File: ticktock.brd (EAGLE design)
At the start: 61 x 67.3 mm, 64 parts, among them IC1 ATMEGA644A, IC2 AD8611RM, IC3 REF200U, J1 AVR_SPI_PRG_6NS, Q1 MOSFET-NCHANNEL2N7002PW, Q2 MOSFET-NCHANNELBSS138, Q3 MOSFET-NCHANNELBSS138, U1 MAX232SOIC16, U2 OSCILLATORSMD, U3 FT232RLSSOP, U4 BMP180, X1 RS232

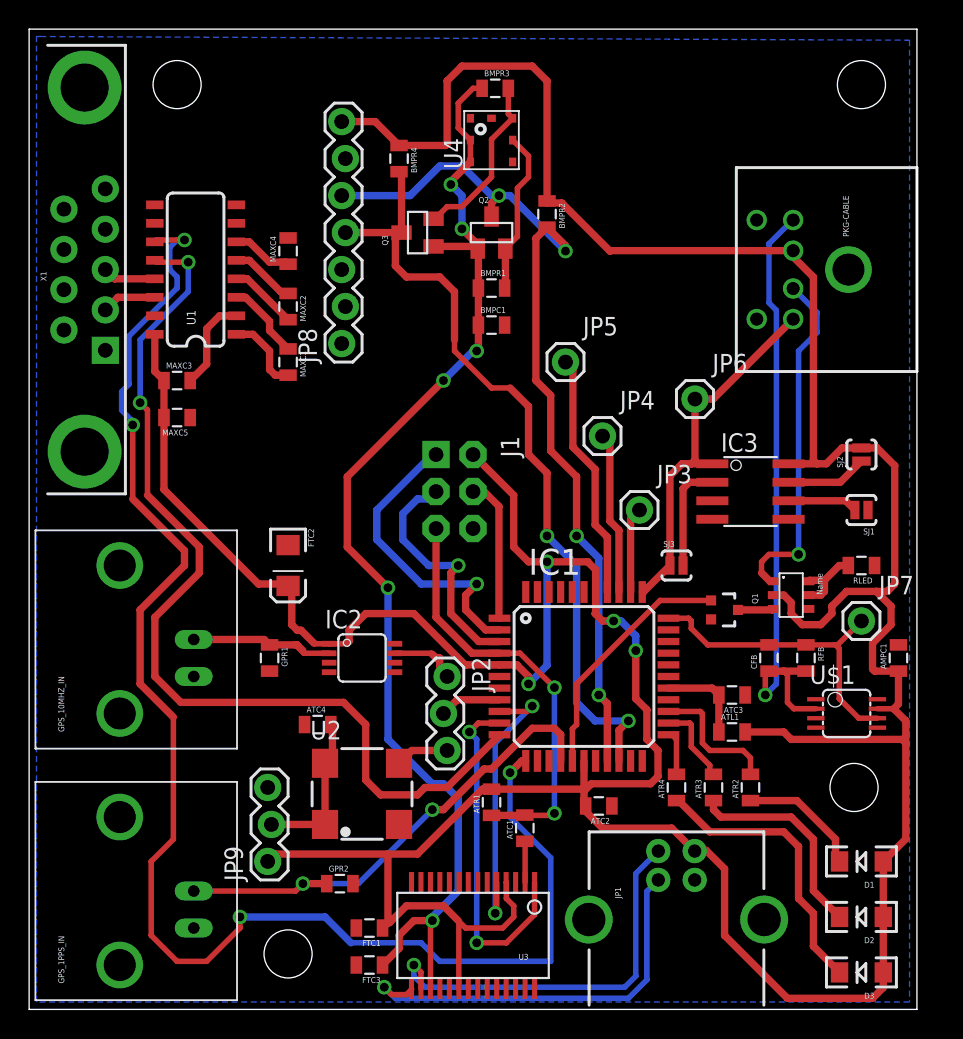
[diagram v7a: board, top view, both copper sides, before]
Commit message: Add top ground plane
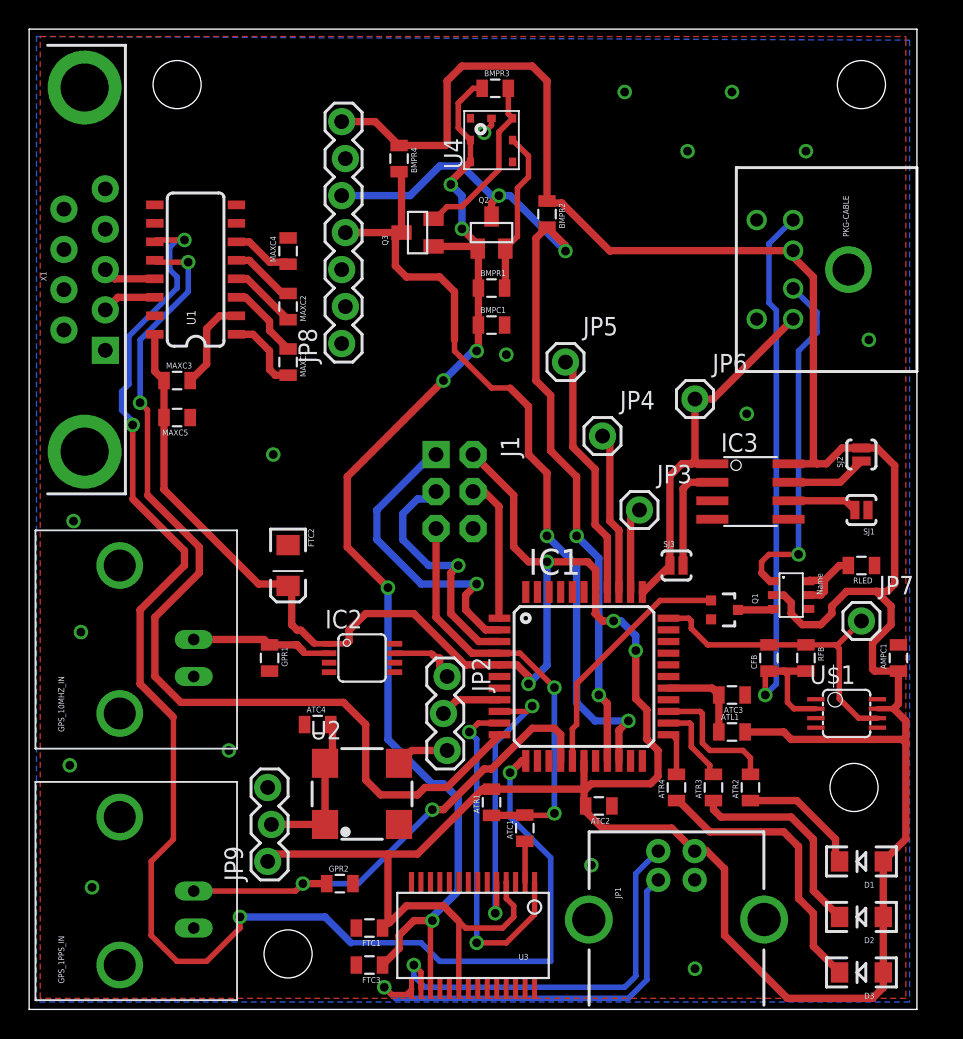
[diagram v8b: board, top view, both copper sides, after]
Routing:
- net GND: track 0.00 -> 1.20 mm, vias 0 -> 15
- added copper zone on layer 1, net GND
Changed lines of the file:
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@@
 <layers>
 <layer number="1" name="Top" color="4" fill="1" visible="yes" active="yes"/>
-<layer number="16" name="Bottom" color="1" fill="1" visible="yes" active="yes"/>
+<layer number="16" name="Bottom" color="1" fill="1" visible="no" active="yes"/>
 <layer number="17" name="Pads" color="2" fill="1" visible="yes" active="yes"/>
 <layer number="18" name="Vias" color="2" fill="1" visible="yes" active="yes"/>
@@
 <vertex x="0.508" y="66.802"/>
 </polygon>
-<wire x1="32.65" y1="46.99" x2="31.75" y2="61.19" width="0" layer="19" extent="1-1"/>
-<wire x1="21.463" y1="45.72" x2="32.65" y2="46.99" width="0" layer="19" extent="1-1"/>
-<wire x1="16.51" y1="23.23" x2="11.303" y2="22.86" width="0" layer="19" extent="1-1"/>
-<wire x1="20.597" y1="23.156" x2="16.51" y2="23.23" width="0" layer="19" extent="1-1"/>
-<wire x1="20.597" y1="23.806" x2="20.597" y2="23.156" width="0" layer="19" extent="1-1"/>
-<wire x1="18.912" y1="19.558" x2="20.597" y2="23.156" width="0" layer="19" extent="1-1"/>
-<wire x1="25.122" y1="23.806" x2="20.597" y2="23.806" width="0" layer="19" extent="1-1"/>
-<wire x1="25.122" y1="23.156" x2="25.122" y2="23.806" width="0" layer="19" extent="1-1"/>
-<wire x1="32.3" y1="22.86" x2="25.122" y2="23.156" width="0" layer="19" extent="1-1"/>
-<wire x1="40.016" y1="13.97" x2="45.7" y2="8.89" width="0" layer="19" extent="1-1"/>
-<wire x1="38.9" y1="17.06" x2="40.016" y2="13.97" width="0" layer="19" extent="1-1"/>
-<wire x1="43.9" y1="22.86" x2="38.9" y2="17.06" width="0" layer="19" extent="1-1"/>
-<wire x1="46.827" y1="26.782" x2="43.9" y2="22.86" width="0" layer="19" extent="1-1"/>
+<polygon width="0.254" layer="1" isolate="0.6096">
+<vertex x="0.762" y="66.802"/>
+<vertex x="60.198" y="66.802"/>
+<vertex x="60.198" y="66.548"/>
+<vertex x="60.198" y="0.762"/>
+<vertex x="0.762" y="0.762"/>
+</polygon>
+<via x="32.766" y="44.958" extent="1-16" drill="0.6"/>
+<wire x1="31.75" y1="61.19" x2="31.75" y2="60.706" width="0.381" layer="1"/>
+<wire x1="31.75" y1="60.706" x2="31.242" y2="60.198" width="0.381" layer="1"/>
+<via x="31.242" y="60.198" extent="1-16" drill="0.6"/>
+<via x="40.894" y="62.992" extent="1-16" drill="0.6"/>
+<via x="48.26" y="62.992" extent="1-16" drill="0.6"/>
+<via x="45.212" y="58.928" extent="1-16" drill="0.6"/>
+<via x="53.34" y="58.928" extent="1-16" drill="0.6"/>
+<via x="57.658" y="45.974" extent="1-16" drill="0.6"/>
+<via x="45.72" y="2.794" extent="1-16" drill="0.6"/>
+<via x="38.608" y="9.906" extent="1-16" drill="0.6"/>
+<via x="13.716" y="17.78" extent="1-16" drill="0.6"/>
+<via x="4.318" y="8.382" extent="1-16" drill="0.6"/>
+<via x="2.794" y="16.764" extent="1-16" drill="0.6"/>
+<via x="3.556" y="25.908" extent="1-16" drill="0.6"/>
+<via x="3.048" y="33.528" extent="1-16" drill="0.6"/>
+<via x="16.764" y="38.1" extent="1-16" drill="0.6"/>
+<wire x1="58.05" y1="30.48" x2="59.69" y2="25.03" width="0" layer="19" extent="1-1"/>
+<wire x1="53.524" y1="27.498" x2="58.05" y2="30.48" width="0" layer="19" extent="1-1"/>
+<wire x1="46.827" y1="26.782" x2="53.524" y2="27.498" width="0" layer="19" extent="1-1"/>
+<wire x1="43.9" y1="22.86" x2="46.827" y2="26.782" width="0" layer="19" extent="1-1"/>
 <wire x1="49.16" y1="21.59" x2="43.9" y2="22.86" width="0" layer="19" extent="1-1"/>
 <wire x1="54.021" y1="19.996" x2="49.16" y2="21.59" width="0" layer="19" extent="1-1"/>
 <wire x1="54.021" y1="19.346" x2="54.021" y2="19.996" width="0" layer="19" extent="1-1"/>
-<wire x1="53.524" y1="27.498" x2="46.827" y2="26.782" width="0" layer="19" extent="1-1"/>
-<wire x1="58.05" y1="30.48" x2="53.524" y2="27.498" width="0" layer="19" extent="1-1"/>
-<wire x1="57.6" y1="34.29" x2="58.05" y2="30.48" width="0" layer="19" extent="1-1"/>
-<wire x1="59.69" y1="25.03" x2="58.05" y2="30.48" width="0" layer="19" extent="1-1"/>
-<wire x1="17.78" y1="52.97" x2="21.463" y2="45.72" width="0" layer="19" extent="1-1"/>
-<wire x1="38.1" y1="28.66" x2="32.3" y2="22.86" width="0" layer="19" extent="1-1"/>
-<wire x1="17.78" y1="31.88" x2="20.597" y2="23.806" width="0" layer="19" extent="1-1"/>
-<wire x1="8.63" y1="47.625" x2="5.23" y2="56.34" width="0" layer="19" extent="1-1"/>
-<wire x1="11.06" y1="40.64" x2="8.63" y2="47.625" width="0" layer="19" extent="1-1"/>
-<wire x1="25.4" y1="12.7" x2="18.912" y2="19.558" width="0" layer="19" extent="1-1"/>
+<wire x1="38.9" y1="17.06" x2="43.9" y2="22.86" width="0" layer="19" extent="1-1"/>
+<wire x1="40.016" y1="13.97" x2="38.9" y2="17.06" width="0" layer="19" extent="1-1"/>
+<wire x1="38.608" y1="9.906" x2="40.016" y2="13.97" width="0" layer="19" extent="1-1"/>
+<wire x1="25.122" y1="23.806" x2="25.122" y2="23.156" width="0" layer="19" extent="1-1"/>
+<wire x1="20.597" y1="23.806" x2="20.597" y2="23.156" width="0" layer="19" extent="1-1"/>
+<wire x1="32.3" y1="22.86" x2="25.122" y2="23.156" width="0" layer="19" extent="1-1"/>
+<wire x1="30.805" y1="8.736" x2="38.608" y2="9.906" width="0" layer="19" extent="1-1"/>
+<wire x1="25.4" y1="12.7" x2="30.805" y2="8.736" width="0" layer="19" extent="1-1"/>
 <wire x1="22.236" y1="8.636" x2="25.4" y2="12.7" width="0" layer="19" extent="1-1"/>
-<wire x1="22.468" y1="5.588" x2="22.236" y2="8.636" width="0" layer="19" extent="1-1"/>
-<wire x1="22.468" y1="3.048" x2="22.468" y2="5.588" width="0" layer="19" extent="1-1"/>
 <wire x1="28.205" y1="1.424" x2="22.468" y2="3.048" width="0" layer="19" extent="1-1"/>
 <wire x1="30.155" y1="1.424" x2="28.205" y2="1.424" width="0" layer="19" extent="1-1"/>
 <wire x1="32.755" y1="1.424" x2="30.155" y2="1.424" width="0" layer="19" extent="1-1"/>
 <wire x1="33.405" y1="1.424" x2="32.755" y2="1.424" width="0" layer="19" extent="1-1"/>
-<wire x1="30.805" y1="8.736" x2="25.4" y2="12.7" width="0" layer="19" extent="1-1"/>
+<wire x1="38.1" y1="28.66" x2="43.9" y2="22.86" width="0" layer="19" extent="1-1"/>
 </signal>
 <signal name="IR_PWM">
@@
 <contactref element="Q3" pad="2"/>
 <contactref element="U4" pad="6"/>
-<wire x1="33.2" y1="61.19" x2="31.75" y2="59.74" width="0.381" layer="1"/>
-<wire x1="31.75" y1="59.74" x2="31.75" y2="57.15" width="0.381" layer="1"/>
-<wire x1="31.75" y1="57.15" x2="29.718" y2="55.118" width="0.381" layer="1"/>
+<wire x1="32.258" y1="57.658" x2="29.718" y2="55.118" width="0.381" layer="1"/>
 <wire x1="29.718" y1="55.118" x2="28.702" y2="55.118" width="0.381" layer="1"/>
 <wire x1="28.702" y1="55.118" x2="27.874" y2="54.29" width="0.381" layer="1"/>
@@
 <wire x1="33.2" y1="61.19" x2="32.904" y2="61.486" width="0.381" layer="1"/>
 <wire x1="32.904" y1="61.486" x2="32.904" y2="63.246" width="0.381" layer="1"/>
+<wire x1="33.2" y1="61.19" x2="32.258" y2="60.248" width="0.381" layer="1"/>
+<wire x1="32.258" y1="60.248" x2="32.258" y2="57.658" width="0.381" layer="1"/>
 </signal>
 <signal name="I2C_SDA">
@@
 <wire x1="55.372" y1="10.438" x2="55.65" y2="10.16" width="0.508" layer="1"/>
 </signal>
+<signal name="N$28">
+<via x="49.276" y="40.894" extent="1-16" drill="0.6"/>
+</signal>
 </signals>
